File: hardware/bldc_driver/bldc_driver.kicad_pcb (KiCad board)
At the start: 4 copper layers, 84.5 x 60 mm, 98 parts, among them J1 Conn_01x03, J10 U, J11 V, J12 W, J2 Conn_01x04, J3 Conn_01x05, J4 Conn_01x06, J5 Conn_01x04, J6 USB_B_Micro, J7 SWD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

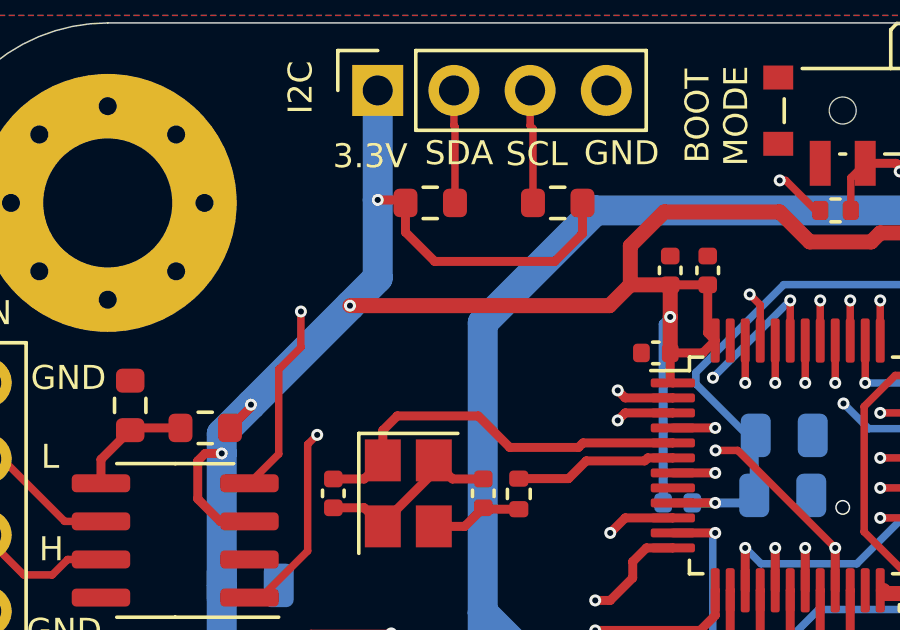
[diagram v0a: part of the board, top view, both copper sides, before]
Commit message: added OSHW logos
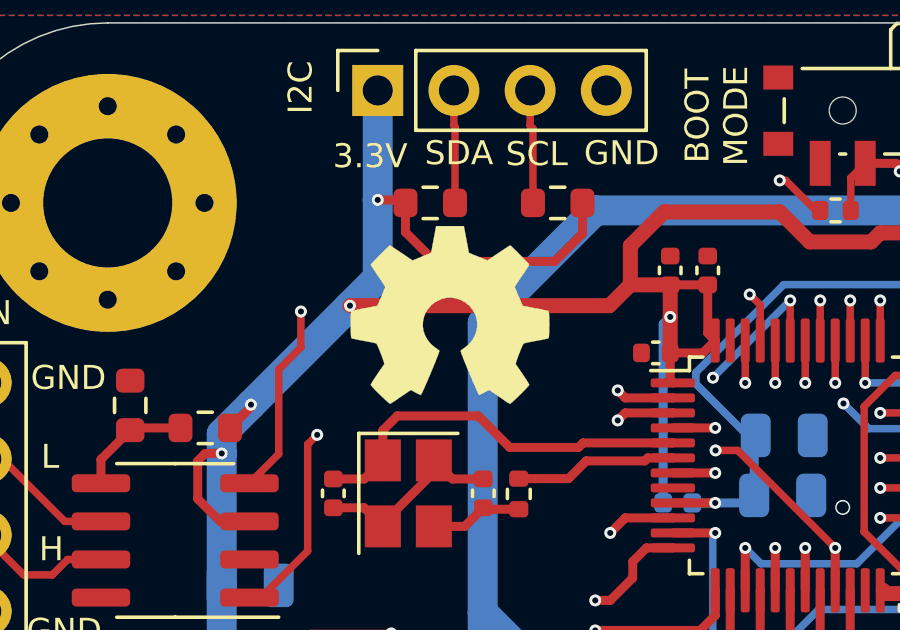
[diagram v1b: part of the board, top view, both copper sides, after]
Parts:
- added REF**: OSHW-Logo_11.4x12mm_SilkScreen, Symbol:OSHW-Logo_11.4x12mm_SilkScreen, B.Cu at (132.3, 133.5)
- added REF**: OSHW-Symbol_6.7x6mm_SilkScreen, Symbol:OSHW-Symbol_6.7x6mm_SilkScreen, F.Cu at (109.9, 133.8)

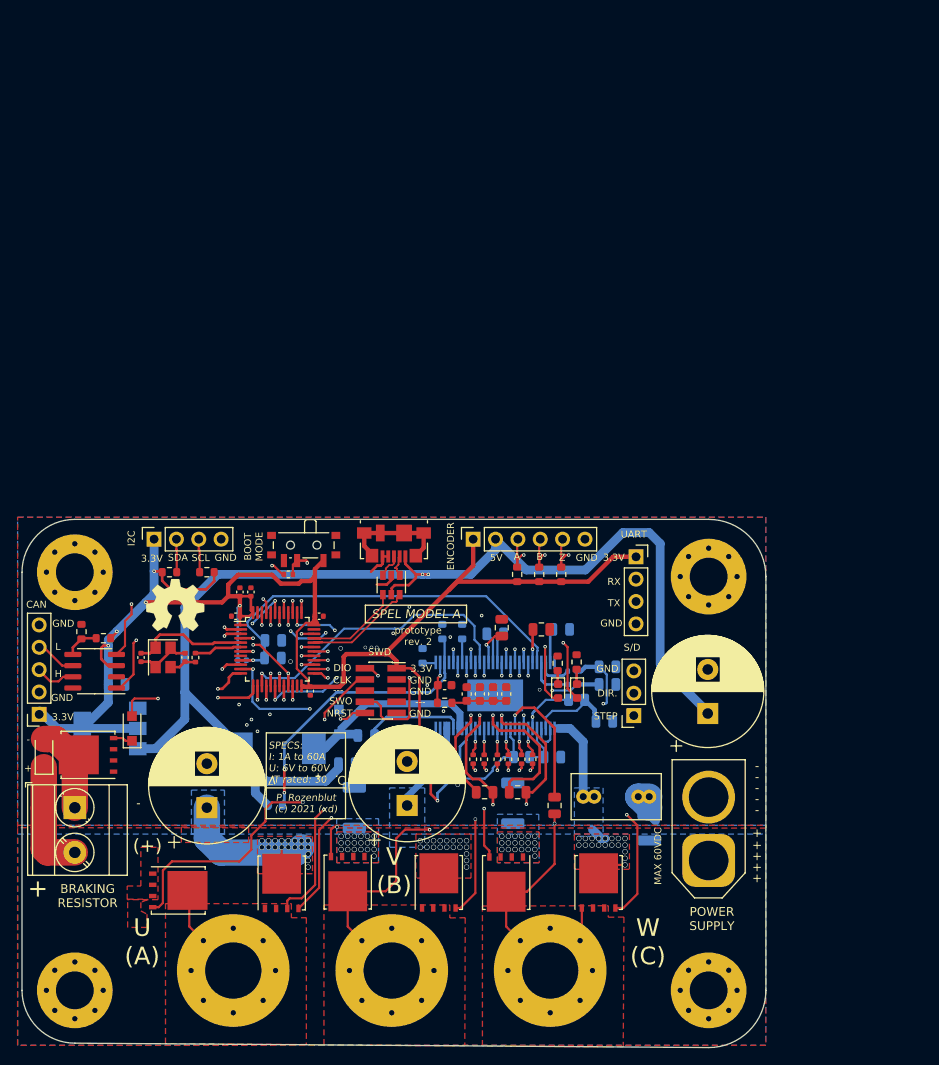
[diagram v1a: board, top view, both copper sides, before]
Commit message: Cosmetic - trace improvements
- correcting 3-way trace intersections
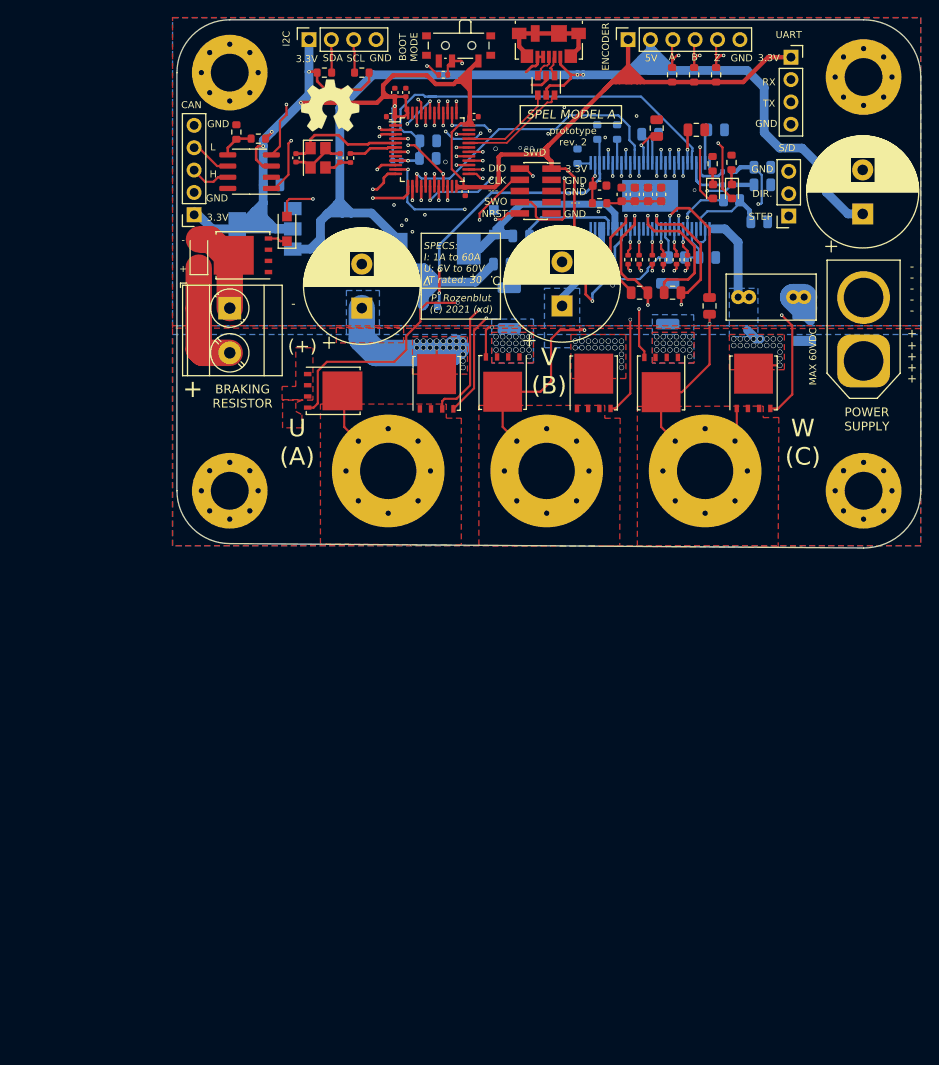
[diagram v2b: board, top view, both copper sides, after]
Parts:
- moved C13 59.4 mm to (149.2, 91.8)
- moved C14 59.4 mm to (188.0, 89.3)
- moved C19 59.4 mm to (164.6, 79.5)
- moved Q1 59.4 mm to (139.6, 108.5)
- moved C1 59.4 mm to (143.8, 78.2)
- moved C10 59.4 mm to (120.8, 86.0)
- moved C11 59.4 mm to (170.3, 94.2)
- moved C15 59.4 mm to (131.1, 100.0)
- moved C16 59.4 mm to (171.3, 79.8)
- moved C17 59.4 mm to (153.8, 99.8)
- moved C18 59.4 mm to (163.8, 80.2)
- moved C20 59.4 mm to (169.1, 79.8)
- moved C21 59.4 mm to (176.6, 84.0)
- moved C22 59.4 mm to (160.6, 87.1)
- moved C23 59.4 mm to (162.7, 98.2)
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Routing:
- net +3V3: track 192.3 -> 225.2 mm
- net +5V: track 138.9 -> 156.0 mm
- net +3.3VA: track 47.0 -> 49.7 mm
- net /control_elements/PH_0: track 64.1 -> 65.2 mm
